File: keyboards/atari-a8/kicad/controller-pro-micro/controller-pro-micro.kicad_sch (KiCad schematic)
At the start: 20 parts, among them J102 Primary Connector, J103 Development Connector, J104 I2C DISPLAY, J105 Jumper Connector, J106 ICSP, SW101 RESET, SW102 SW_DIP_x01, U101 ProMicro, U102 7402, U103 74LS08

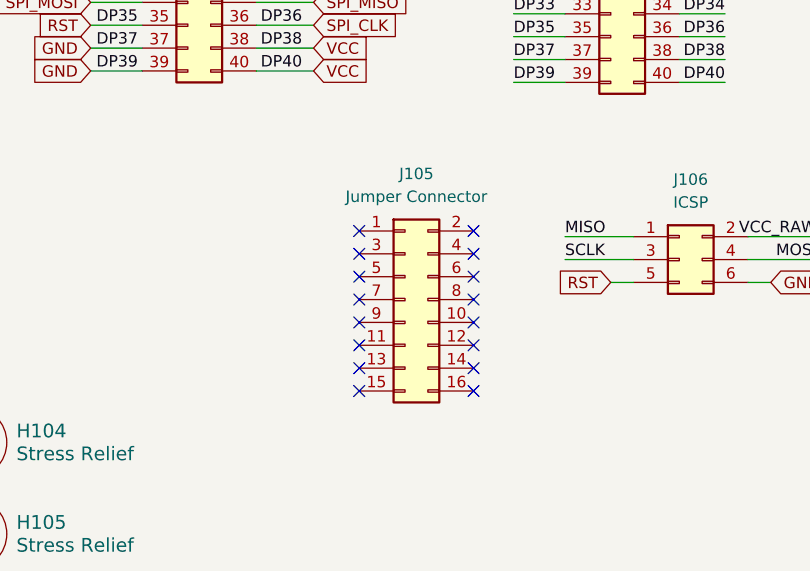
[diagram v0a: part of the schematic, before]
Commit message: Renamed the pro micro controller
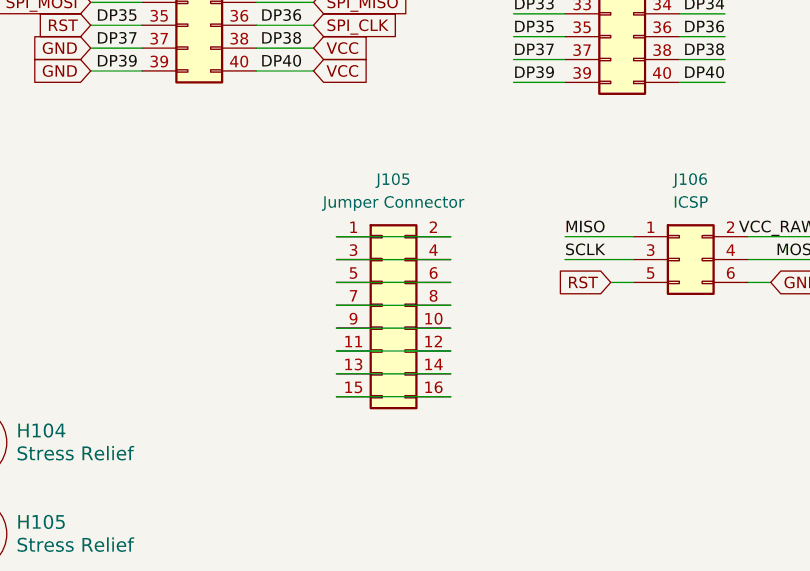
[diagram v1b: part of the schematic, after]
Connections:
- net at J105.1 (Pin_1): now also J105.2 (Pin_2)
- net at J105.10 (Pin_10): now also J105.9 (Pin_9)
- net at J105.11 (Pin_11): now also J105.12 (Pin_12)
- net at J105.13 (Pin_13): now also J105.14 (Pin_14)
- net at J105.15 (Pin_15): now also J105.16 (Pin_16)
- net at J105.3 (Pin_3): now also J105.4 (Pin_4)
- net at J105.5 (Pin_5): now also J105.6 (Pin_6)
- net at J105.7 (Pin_7): now also J105.8 (Pin_8)
- no-connect marks 19 -> 3
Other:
- moved on the sheet: J105
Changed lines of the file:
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@@
   (junction (at 37.465 167.005) (diameter 0) (color 0 0 0 0)
   )
-  (no_connect (at 226.06 93.345))
-  (no_connect (at 238.76 108.585))
-  (no_connect (at 226.06 106.045))
-  (no_connect (at 238.76 103.505))
-  (no_connect (at 226.06 95.885))
   (no_connect (at 89.535 146.05))
-  (no_connect (at 226.06 103.505))
-  (no_connect (at 238.76 100.965))
-  (no_connect (at 226.06 108.585))
   (no_connect (at 89.535 167.005))
-  (no_connect (at 238.76 93.345))
-  (no_connect (at 238.76 98.425))
-  (no_connect (at 226.06 100.965))
-  (no_connect (at 238.76 106.045))
-  (no_connect (at 238.76 111.125))
-  (no_connect (at 238.76 95.885))
-  (no_connect (at 226.06 98.425))
   (no_connect (at 78.74 35.56))
-  (no_connect (at 226.06 111.125))
   (wire (pts (xy 37.465 146.05) (xy 53.975 146.05))
     (stroke (width 0) (type default))
@@
     (stroke (width 0) (type default))
   )
+  (wire (pts (xy 223.52 111.76) (xy 236.22 111.76))
+    (stroke (width 0) (type default))
+  )
   (wire (pts (xy 214.63 34.925) (xy 220.98 34.925))
     (stroke (width 0) (type default))
@@
     (stroke (width 0) (type default))
   )
+  (wire (pts (xy 223.52 101.6) (xy 236.22 101.6))
+    (stroke (width 0) (type default))
+  )
   (wire (pts (xy 243.205 46.355) (xy 248.92 46.355))
     (stroke (width 0) (type default))
@@
     (stroke (width 0) (type default))
   )
+  (wire (pts (xy 223.52 93.98) (xy 236.22 93.98))
+    (stroke (width 0) (type default))
+  )
   (wire (pts (xy 214.63 40.005) (xy 220.98 40.005))
     (stroke (width 0) (type default))
@@
     (stroke (width 0) (type default))
   )
+  (wire (pts (xy 223.52 104.14) (xy 236.22 104.14))
+    (stroke (width 0) (type default))
+  )
   (wire (pts (xy 261.62 76.835) (xy 266.7 76.835))
     (stroke (width 0) (type default))
@@
     (stroke (width 0) (type default))
   )
+  (wire (pts (xy 223.52 99.06) (xy 236.22 99.06))
+    (stroke (width 0) (type default))
+  )
   (wire (pts (xy 196.215 73.025) (xy 201.93 73.025))
     (stroke (width 0) (type default))
   )
+  (wire (pts (xy 223.52 96.52) (xy 236.22 96.52))
+    (stroke (width 0) (type default))
+  )
   (wire (pts (xy 118.11 157.48) (xy 118.11 160.655))
     (stroke (width 0) (type default))
@@
     (stroke (width 0) (type default))
   )
+  (wire (pts (xy 223.52 106.68) (xy 236.22 106.68))
+    (stroke (width 0) (type default))
+  )
   (wire (pts (xy 243.205 59.055) (xy 248.92 59.055))
     (stroke (width 0) (type default))
@@
   )
   (wire (pts (xy 196.215 37.465) (xy 201.93 37.465))
+    (stroke (width 0) (type default))
+  )
+  (wire (pts (xy 223.52 109.22) (xy 236.22 109.22))
     (stroke (width 0) (type default))
   )
@@
     (pin "1")
     (instances
-      (project "atari-keyboard"
+      (project "controller-pro-micro"
         (path "/f6a334f3-ee33-4c56-a7bb-b961693d3d0e"
           (reference "SW102") (unit 1)
@@
     )
     (instances
-      (project "atari-keyboard"
+      (project "controller-pro-micro"
         (path "/f6a334f3-ee33-4c56-a7bb-b961693d3d0e"
           (reference "H102") (unit 1)
@@
     (pin "2")
     (instances
-      (project "atari-keyboard"
+      (project "controller-pro-micro"
         (path "/f6a334f3-ee33-4c56-a7bb-b961693d3d0e"
           (reference "U103") (unit 5)
@@
     )
     (instances
-      (project "atari-keyboard"
+      (project "controller-pro-micro"
         (path "/f6a334f3-ee33-4c56-a7bb-b961693d3d0e"
           (reference "H105") (unit 1)
@@
     (pin "2")
     (instances
-      (project "atari-keyboard"
+      (project "controller-pro-micro"
         (path "/f6a334f3-ee33-4c56-a7bb-b961693d3d0e"
           (reference "U103") (unit 3)
@@
     )
   )
-  (symbol (lib_id "Connector_Generic:Conn_02x08_Odd_Even") (at 231.14 100.965 0) (unit 1)
-    (in_bom yes) (on_board yes) (dnp no) (fields_autoplaced)
-    (property "Reference" "J105" (at 232.41 86.995 0)
-      (effects (font (size 1.27 1.27)))
-    )
-    (property "Value" "Jumper Connector" (at 232.41 89.535 0)
-      (effects (font (size 1.27 1.27)))
-    )
-    (property "Footprint" "Connector_PinHeader_2.54mm:PinHeader_2x08_P2.54mm_Vertical" (at 231.14 100.965 0)
-      (effects (font (size 1.27 1.27)) hide)
-    )
-    (property "Datasheet" "~" (at 231.14 100.965 0)
+  (symbol (lib_id "Connector_Generic:Conn_02x08_Odd_Even") (at 228.6 101.6 0) (unit 1)
+    (in_bom yes) (on_board yes) (dnp no) (fields_autoplaced)
+    (property "Reference" "J105" (at 229.87 87.63 0)
+      (effects (font (size 1.27 1.27)))
+    )
+    (property "Value" "Jumper Connector" (at 229.87 90.17 0)
+      (effects (font (size 1.27 1.27)))
+    )
+    (property "Footprint" "Connector_PinHeader_2.54mm:PinHeader_2x08_P2.54mm_Vertical" (at 228.6 101.6 0)
+      (effects (font (size 1.27 1.27)) hide)
+    )
+    (property "Datasheet" "~" (at 228.6 101.6 0)
       (effects (font (size 1.27 1.27)) hide)
     )
@@
     (pin "3")
     (instances
-      (project "atari-keyboard"
+      (project "controller-pro-micro"
         (path "/f6a334f3-ee33-4c56-a7bb-b961693d3d0e"
           (reference "J105") (unit 1)
@@
     )
     (instances
-      (project "atari-keyboard"
+      (project "controller-pro-micro"
         (path "/f6a334f3-ee33-4c56-a7bb-b961693d3d0e"
           (reference "H104") (unit 1)
@@
     (pin "2")
     (instances
-      (project "atari-keyboard"
+      (project "controller-pro-micro"
         (path "/f6a334f3-ee33-4c56-a7bb-b961693d3d0e"
           (reference "D101") (unit 1)
@@
     (pin "5")
     (instances
-      (project "atari-keyboard"
+      (project "controller-pro-micro"
         (path "/f6a334f3-ee33-4c56-a7bb-b961693d3d0e"
           (reference "U102") (unit 5)
@@
     (pin "1")
     (instances
-      (project "atari-keyboard"
+      (project "controller-pro-micro"
         (path "/f6a334f3-ee33-4c56-a7bb-b961693d3d0e"
           (reference "C102") (unit 1)
@@
     (pin "5")
     (instances
-      (project "atari-keyboard"
+      (project "controller-pro-micro"
         (path "/f6a334f3-ee33-4c56-a7bb-b961693d3d0e"
           (reference "U102") (unit 1)
@@
     (pin "2")
     (instances
-      (project "atari-keyboard"
+      (project "controller-pro-micro"
         (path "/f6a334f3-ee33-4c56-a7bb-b961693d3d0e"
           (reference "U103") (unit 1)
@@
     (pin "2")
     (instances
-      (project "atari-keyboard"
+      (project "controller-pro-micro"
         (path "/f6a334f3-ee33-4c56-a7bb-b961693d3d0e"
           (reference "R101") (unit 1)
@@
     (pin "2")
     (instances
-      (project "atari-keyboard"
+      (project "controller-pro-micro"
         (path "/f6a334f3-ee33-4c56-a7bb-b961693d3d0e"
           (reference "U103") (unit 4)
@@
     )
     (instances
-      (project "atari-keyboard"
+      (project "controller-pro-micro"
         (path "/f6a334f3-ee33-4c56-a7bb-b961693d3d0e"
           (reference "H101") (unit 1)
@@
     (pin "20")
     (instances
-      (project "atari-keyboard"
+      (project "controller-pro-micro"
         (path "/f6a334f3-ee33-4c56-a7bb-b961693d3d0e"
           (reference "U101") (unit 1)
@@
     )
     (instances
-      (project "atari-keyboard"
+      (project "controller-pro-micro"
         (path "/f6a334f3-ee33-4c56-a7bb-b961693d3d0e"
           (reference "H103") (unit 1)
@@
     (pin "4")
     (instances
-      (project "atari-keyboard"
+      (project "controller-pro-micro"
         (path "/f6a334f3-ee33-4c56-a7bb-b961693d3d0e"
           (reference "J104") (unit 1)
@@
     (pin "5")
     (instances
-      (project "atari-keyboard"
+      (project "controller-pro-micro"
         (path "/f6a334f3-ee33-4c56-a7bb-b961693d3d0e"
           (reference "U102") (unit 4)
@@
     (pin "1")
     (instances
-      (project "atari-keyboard"
+      (project "controller-pro-micro"
         (path "/f6a334f3-ee33-4c56-a7bb-b961693d3d0e"
           (reference "C101") (unit 1)
@@
     (pin "5")
     (instances
-      (project "atari-keyboard"
+      (project "controller-pro-micro"
         (path "/f6a334f3-ee33-4c56-a7bb-b961693d3d0e"
           (reference "U102") (unit 3)
@@
     (pin "2")
     (instances
-      (project "atari-keyboard"
+      (project "controller-pro-micro"
         (path "/f6a334f3-ee33-4c56-a7bb-b961693d3d0e"
           (reference "U103") (unit 2)
@@
     )
     (instances
-      (project "atari-keyboard"
+      (project "controller-pro-micro"
         (path "/f6a334f3-ee33-4c56-a7bb-b961693d3d0e"
           (reference "H106") (unit 1)
@@
     (pin "36")
     (instances
-      (project "atari-keyboard"
+      (project "controller-pro-micro"
         (path "/f6a334f3-ee33-4c56-a7bb-b961693d3d0e"
           (reference "J102") (unit 1)
@@
     (pin "1")
     (instances
-      (project "atari-keyboard"
+      (project "controller-pro-micro"
         (path "/f6a334f3-ee33-4c56-a7bb-b961693d3d0e"
           (reference "SW101") (unit 1)
@@
     (pin "5")
     (instances
-      (project "atari-keyboard"
+      (project "controller-pro-micro"
         (path "/f6a334f3-ee33-4c56-a7bb-b961693d3d0e"
           (reference "J106") (unit 1)
@@
     (pin "5")
     (instances
-      (project "atari-keyboard"
+      (project "controller-pro-micro"
         (path "/f6a334f3-ee33-4c56-a7bb-b961693d3d0e"
           (reference "U102") (unit 2)
@@
     (pin "36")
     (instances
-      (project "atari-keyboard"
+      (project "controller-pro-micro"
         (path "/f6a334f3-ee33-4c56-a7bb-b961693d3d0e"
           (reference "J103") (unit 1)
